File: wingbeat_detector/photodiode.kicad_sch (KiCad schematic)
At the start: 13 parts, among them J3 CONN_UMC_JACK_SMD, U4 OPA381, U5 TSV630IQ1T

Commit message: Finished layout for v3.0
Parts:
- J3: value CONN_UMC_JACK_SMD -> UMC_JACK_SMD
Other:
- company: Howard Hughes Medical Institute -> Peter Polidoro
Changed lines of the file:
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@@
   (title_block
     (title "wingbeat_detector")
-    (date "2023-03-22")
+    (date "2023-03-23")
     (rev "3.0")
-    (company "Howard Hughes Medical Institute")
+    (company "Peter Polidoro")
   )
   (junction (at 186.69 111.76) (diameter 0) (color 0 0 0 0)
@@
       (effects (font (size 1.27 1.27)) (justify left))
     )
-    (property "Value" "CONN_UMC_JACK_SMD" (at 237.871 96.52 90)
-      (effects (font (size 1.27 1.27)) hide)
-    )
+    (property "Value" "UMC_JACK_SMD" (at 237.871 96.52 90)
+      (effects (font (size 1.27 1.27)) hide)
+    )

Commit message: More progress towards v4
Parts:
- removed C9: 0.1uF, Janelia:C_0402_1005Metric, symbol Janelia:C_0.1uF_0402
- removed J3: UMC_JACK_SMD, Janelia:UMC_AMPHENOL_A-1JB, symbol Janelia:CONN_UMC_JACK_SMD
- removed R2: 23.2k, Janelia:R_0402_1005Metric, symbol Janelia:R_23.2k_0402
- removed R3: 49.9k, Janelia:R_0402_1005Metric, symbol Janelia:R_49.9k_0402
- removed RV2: 500k, Janelia:Potentiometer_Bourns_3223W_Vertical, symbol Janelia:R_Potentiometer_500k_3.9x3.18mm_11turn_Vertical
- removed U5: TSV630IQ1T, Janelia:PSON40P120X130X50-6N, symbol Janelia:TSV630IQ1T
- added R14: GAIN0, Janelia:R_1206_3216Metric, symbol Janelia:R_150k_1206
- renumbered C9 to C10, R3 to R11, R3 to R12, R3 to R13
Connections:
- net PHOTODIODE_RAW: now also R14.2
- net at C11.1, D1.1 (K), U4.2 (-): now also R14.1
- no-connect marks 1 -> 0
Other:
- note added: "R = (5V - 0.6V)/90uA = 48.8k > 48.8k to increase GAIN0"
- note removed: "49.9k/(23.2k + 49.9k) = 0.68 0.68 * (5V - 0.6V) = 3V Max"
- note removed: "RF = (5V - 0.6V)/90uA = 48.8k 1 turn of potentiometer ~ 50k > 1 turns to increase gain"
- moved on the sheet: C11

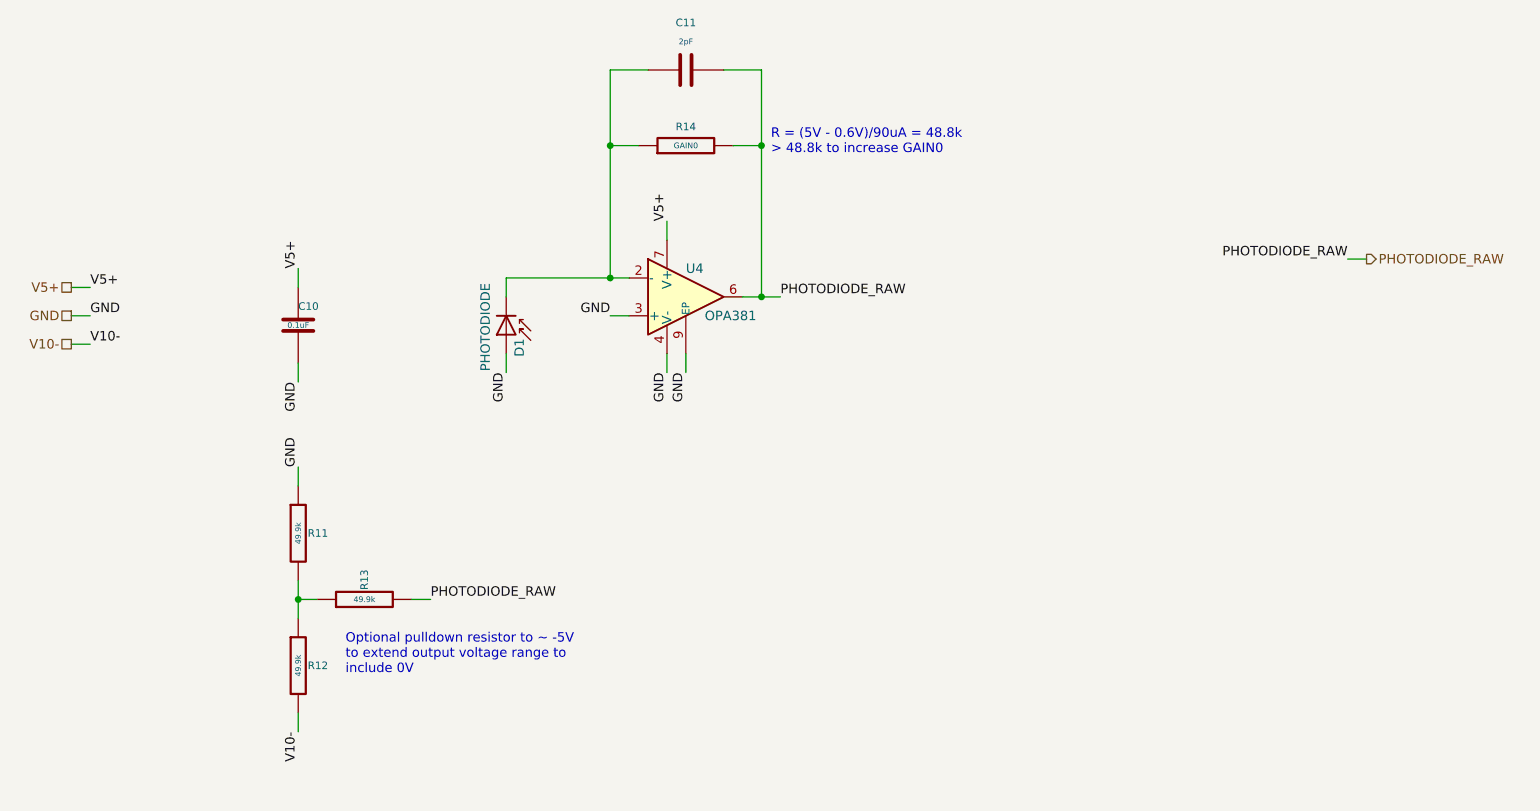
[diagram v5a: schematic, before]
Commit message: First attempt at routing
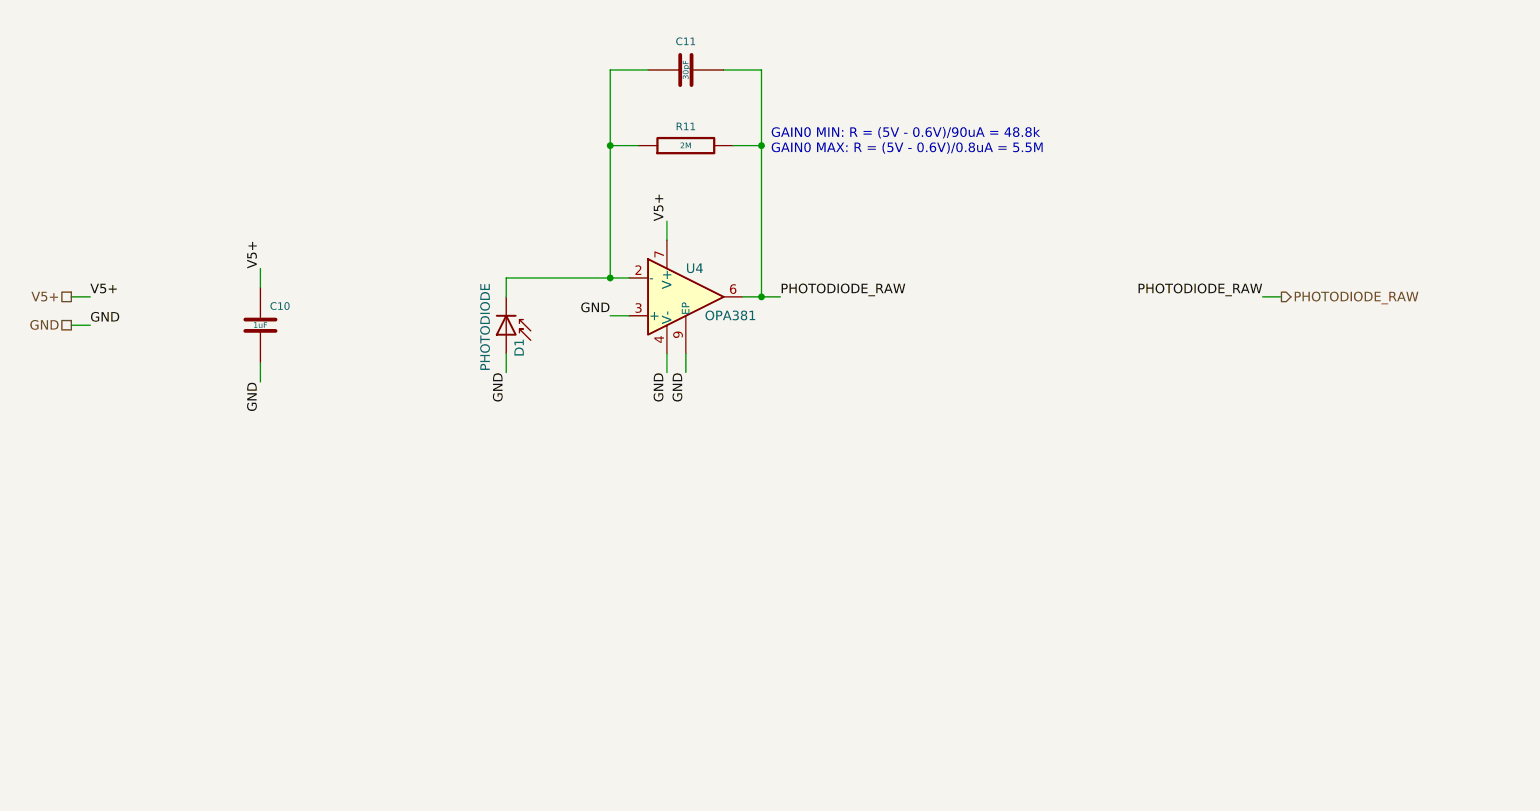
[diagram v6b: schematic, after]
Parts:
- removed C10: 0.1uF, Janelia:C_0402_1005Metric, symbol Janelia:C_0.1uF_0402
- removed C11: 2pF, Janelia:C_0402_1005Metric, symbol Janelia:C_2pF_0402
- removed R11, R12, R13: 49.9k, Janelia:R_0402_1005Metric, symbol Janelia:R_49.9k_0402
- removed R14: GAIN0, Janelia:R_1206_3216Metric, symbol Janelia:R_150k_1206
- added C10: 1uF, Janelia:C_0402_1005Metric, symbol Janelia:C_1uF_35V_0402
- added C11: 30pF, Janelia:C_0402_1005Metric, symbol Janelia:C_30pF_50V_0402
- added R11: 2M, Janelia:R_1206_3216Metric, symbol Janelia:R_2M_1206
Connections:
- net GND: now also C10.2
- net PHOTODIODE_RAW: now also C11.2, R11.2
- net V5+: now also C10.1
- net at D1.1 (K), U4.2 (-): now also C11.1, R11.1
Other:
- note added: "GAIN0 MIN: R = (5V - 0.6V)/90uA = 48.8k GAIN0 MAX: R = (5V - 0.6V)/0.8uA = 5.5M"
- note removed: "Optional pulldown resistor to ~ -5V to extend output voltage range to include 0V"
- note removed: "R = (5V - 0.6V)/90uA = 48.8k > 48.8k to increase GAIN0"

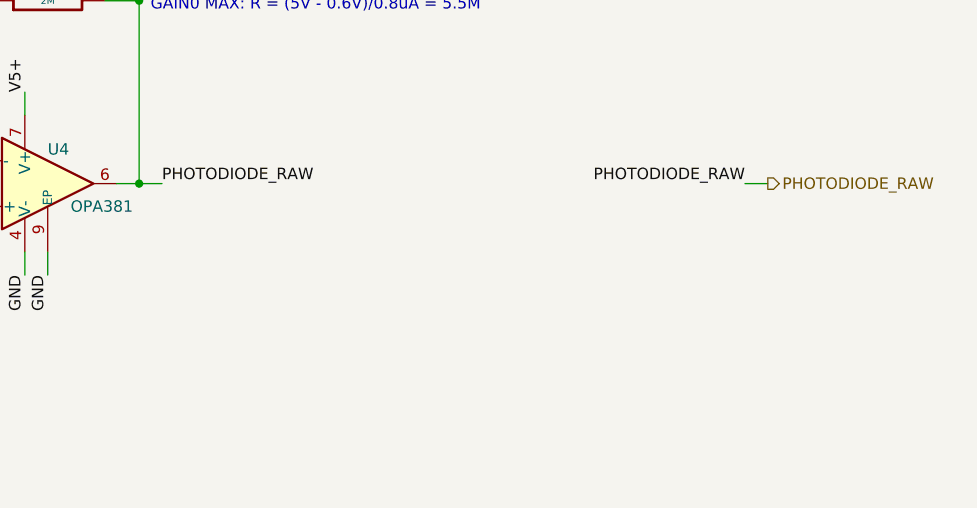
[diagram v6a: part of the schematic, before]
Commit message: Adjust tracks and zones
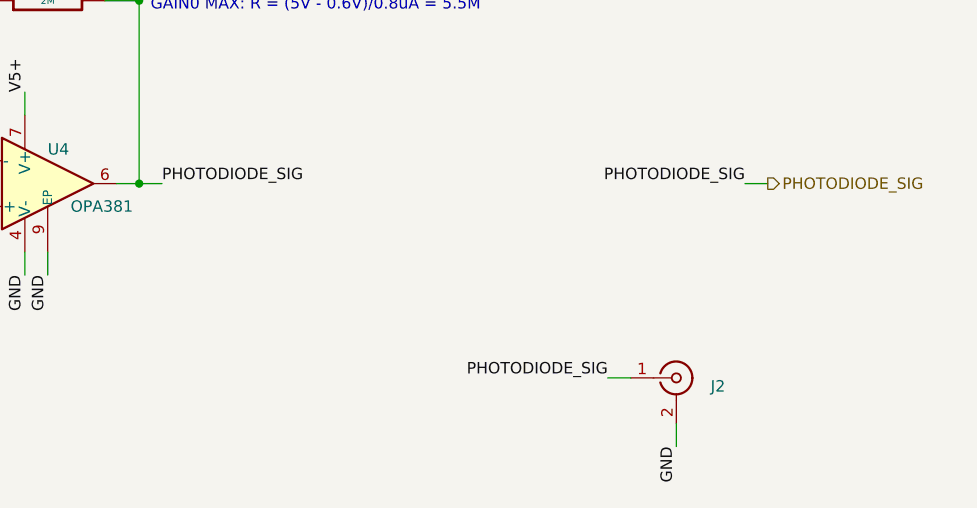
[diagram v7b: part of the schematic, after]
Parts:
- added J2: UMC_JACK_SMD, Janelia:UMC_AMPHENOL_A-1JB, symbol Janelia:CONN_UMC_JACK_SMD
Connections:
- net GND: now also J2.2 (Ext)
- net PHOTODIODE_RAW renamed PHOTODIODE_SIG
- net PHOTODIODE_SIG: now also J2.1 (In)
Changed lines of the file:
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@@
   (title_block
     (title "wingbeat_detector")
-    (date "2023-12-11")
+    (date "2023-12-12")
     (rev "4.0")
     (company "Peter Polidoro")
@@
     (stroke (width 0) (type default))
   )
+  (wire (pts (xy 203.2 106.68) (xy 200.66 106.68))
+    (stroke (width 0) (type default))
+  )
   (wire (pts (xy 81.28 93.98) (xy 81.28 96.52))
     (stroke (width 0) (type default))
@@
   )
   (wire (pts (xy 128.27 54.61) (xy 128.27 64.77))
+    (stroke (width 0) (type default))
+  )
+  (wire (pts (xy 208.28 111.76) (xy 208.28 114.3))
     (stroke (width 0) (type default))
   )
@@
     (effects (font (size 1.27 1.27)) (justify left bottom))
   )
+  (label "GND" (at 208.28 114.3 270) (fields_autoplaced)
+    (effects (font (size 1.27 1.27)) (justify right bottom))
+  )
   (label "GND" (at 114.3 95.25 270) (fields_autoplaced)
     (effects (font (size 1.27 1.27)) (justify right bottom))
@@
     (effects (font (size 1.27 1.27)) (justify left bottom))
   )
-  (label "PHOTODIODE_RAW" (at 151.13 85.09 0) (fields_autoplaced)
+  (label "PHOTODIODE_SIG" (at 151.13 85.09 0) (fields_autoplaced)
     (effects (font (size 1.27 1.27)) (justify left bottom))
   )
@@
     (effects (font (size 1.27 1.27)) (justify left bottom))
   )
+  (label "PHOTODIODE_SIG" (at 200.66 106.68 180) (fields_autoplaced)
+    (effects (font (size 1.27 1.27)) (justify right bottom))
+  )
   (label "GND" (at 135.89 95.25 270) (fields_autoplaced)
     (effects (font (size 1.27 1.27)) (justify right bottom))
@@
     (effects (font (size 1.27 1.27)) (justify left bottom))
   )
-  (label "PHOTODIODE_RAW" (at 215.9 85.09 180) (fields_autoplaced)
+  (label "PHOTODIODE_SIG" (at 215.9 85.09 180) (fields_autoplaced)
     (effects (font (size 1.27 1.27)) (justify right bottom))
   )
@@
     (effects (font (size 1.27 1.27)) (justify right bottom))
   )
-  (hierarchical_label "PHOTODIODE_RAW" (shape output) (at 218.44 85.09 0) (fields_autoplaced)
+  (hierarchical_label "PHOTODIODE_SIG" (shape output) (at 218.44 85.09 0) (fields_autoplaced)
     (effects (font (size 1.27 1.27)) (justify left))
   )
@@
     )
   )
+  (symbol (lib_id "Janelia:CONN_UMC_JACK_SMD") (at 208.28 106.68 0) (unit 1)
+    (in_bom yes) (on_board yes) (dnp no) (fields_autoplaced)
+    (property "Reference" "J2" (at 212.09 107.6082 0)
+      (effects (font (size 1.27 1.27)) (justify left))
+    )
+    (property "Value" "UMC_JACK_SMD" (at 211.201 106.68 90)
+      (effects (font (size 1.27 1.27)) hide)
+    )
+    (property "Footprint" "Janelia:UMC_AMPHENOL_A-1JB" (at 208.28 93.98 0)
+      (effects (font (size 1.27 1.27)) hide)
+    )
+    (property "Datasheet" "" (at 208.28 106.68 0)
+      (effects (font (size 1.27 1.27)) hide)
+    )
+    (property "Manufacturer" "Amphenol RF" (at 208.28 96.52 0)
+      (effects (font (size 1.27 1.27)) hide)
+    )
+    (property "Manufacturer Part Number" "A-1JB" (at 208.28 121.92 0)
+      (effects (font (size 1.27 1.27)) hide)
+    )
+    (property "Vendor" "Digi-Key" (at 208.28 124.46 0)
+      (effects (font (size 1.27 1.27)) hide)
+    )
+    (property "Vendor Part Number" "115-A-1JBCT-ND" (at 208.28 119.38 0)
+      (effects (font (size 1.27 1.27)) hide)
+    )
+    (property "Description" "CONN UMC JACK STR 50 OHM SMD" (at 208.28 91.44 0)
+      (effects (font (size 1.27 1.27)) hide)
+    )
+    (property "Sim.Enable" "0" (at 208.28 106.68 0)
+      (effects (font (size 1.27 1.27)) hide)
+    )
+    (pin "1")
+    (pin "2")
+    (instances
+      (project "wingbeat_detector"
+        (path "/cc457ebc-4af6-4663-b19f-8cb38f061cb4"
+          (reference "J2") (unit 1)
+        )
+        (path "/cc457ebc-4af6-4663-b19f-8cb38f061cb4/6cde90e6-6156-42e3-aaac-c45ad2bfab8b"
+          (reference "J2") (unit 1)
+        )
+        (path "/cc457ebc-4af6-4663-b19f-8cb38f061cb4/6f9841bf-b0ef-48ff-bf2c-2bd611c72bf3"
+          (reference "J3") (unit 1)
+        )
+      )
+    )
+  )
   (symbol (lib_id "Janelia:PHOTODIODE_940nm_RADIAL_RA_SMD_BRIGHT") (at 114.3 90.17 270) (unit 1)
     (in_bom yes) (on_board yes) (dnp no)
@@
       (effects (font (size 1.27 1.27)) hide)
     )
+    (property "Sim.Enable" "0" (at 114.3 90.17 0)
+      (effects (font (size 1.27 1.27)) hide)
+    )
